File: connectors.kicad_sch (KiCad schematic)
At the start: 22 parts, among them J1 RPi_GPIO, J10 ToF1_Sensor, J11 ToF2_Sensor, J12 ToF3_Sensor, J13 ToF4_Sensor, J14 ToF5_Sensor, J15 ToF6_Sensor, J16 SPI_Interface, J17 UART_Interface, J18 Fan_Interface, J2 Motor_L, J3 Motor_R, J4 B_Cell_3, J5 B_Cell_2, J6 B_Cell_1, J7 SW, J8 Temp_Sensor, J9 IMU_Sensor

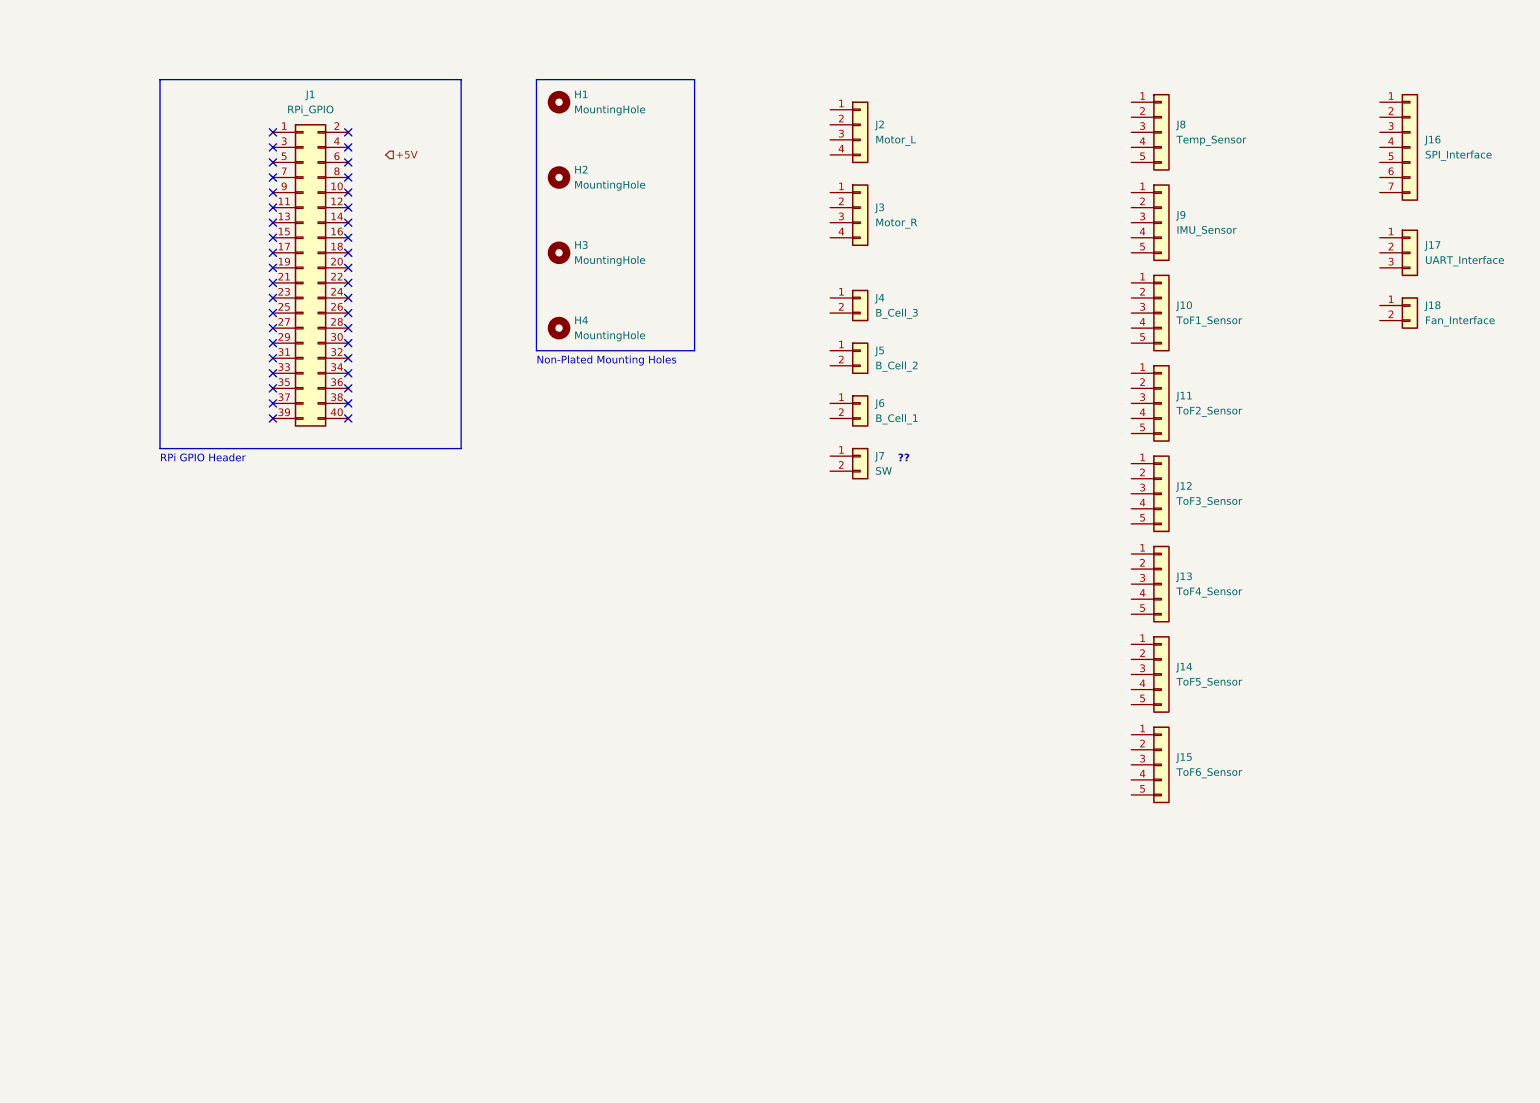
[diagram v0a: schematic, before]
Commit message: Finished motor drivers schematic
Still need to connect all the connectors and sort out old unused connections
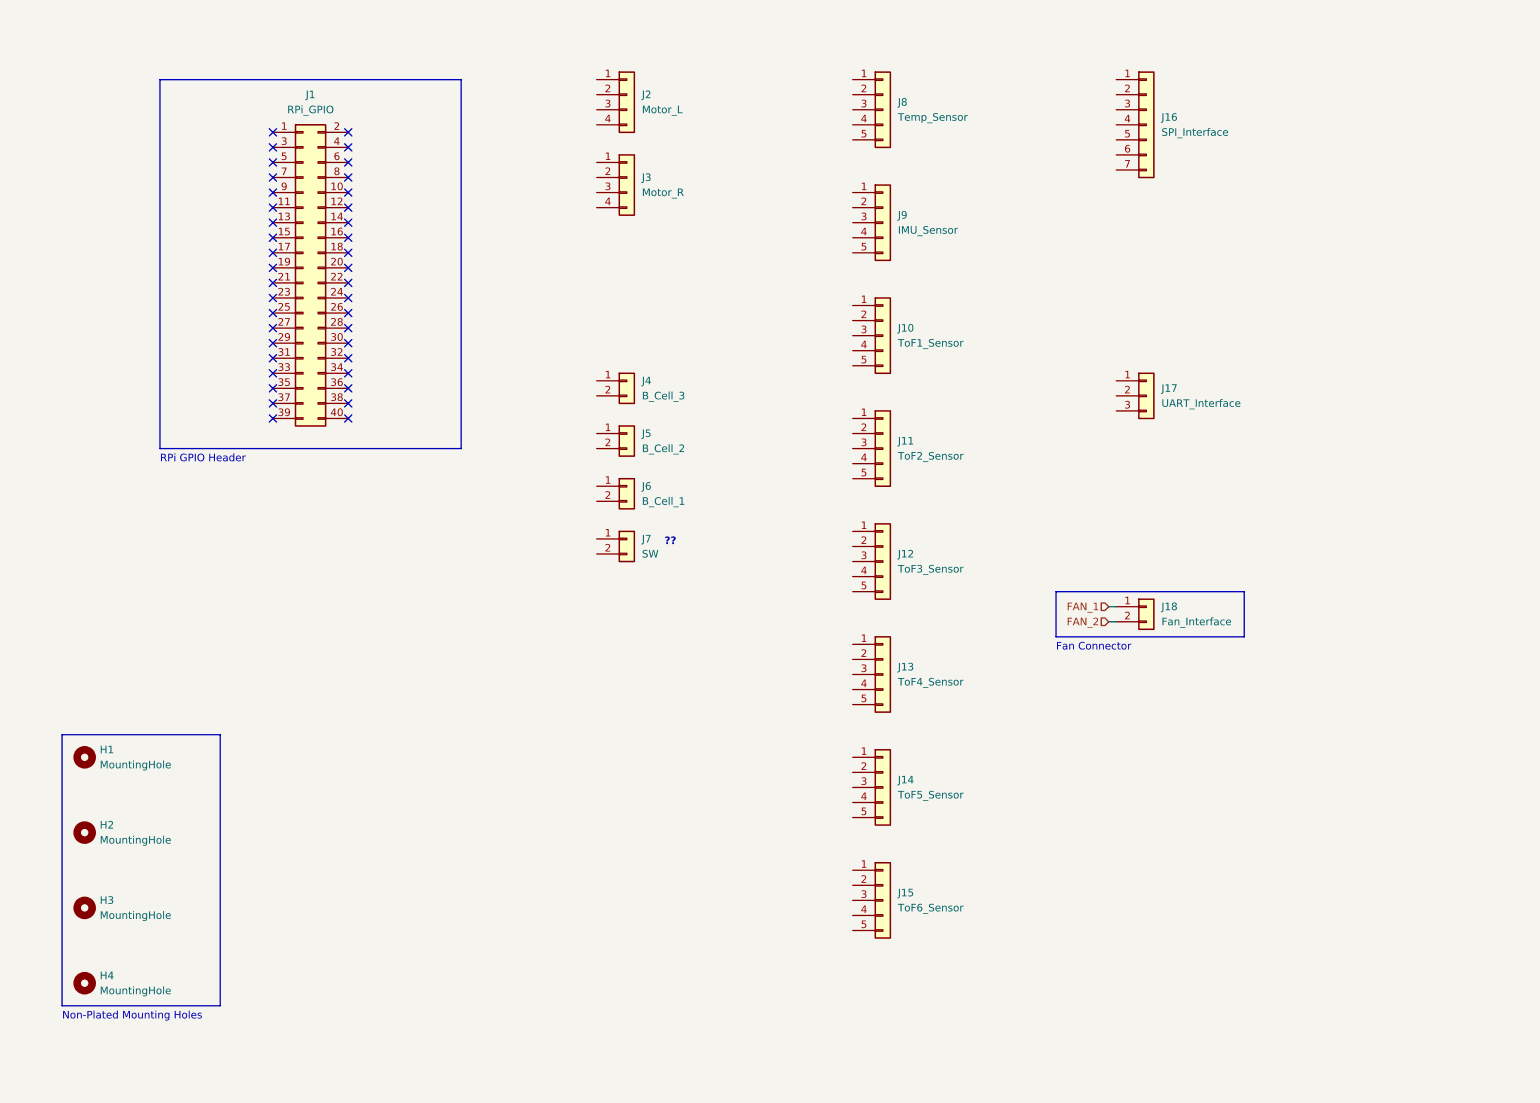
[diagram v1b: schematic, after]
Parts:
- J10, J11, J12, J13, J14, J15, J8, J9: footprint Connector_Molex:Molex_PicoBlade_53047-0510_1x05_P1.25mm_Vertical -> parts:SHDR5W27P0X125_1X5_800X320X440P
- J16: footprint Connector_Molex:Molex_PicoBlade_53047-0710_1x07_P1.25mm_Vertical -> parts:530470710
- J2, J3: footprint Connector_Molex:Molex_Micro-Fit_3.0_43650-0415_1x04_P3.00mm_Vertical -> parts:43650-04YY_151617
- J4, J5, J6, J7: footprint Connector_Molex:Molex_Micro-Fit_3.0_43045-0212_2x01_P3.00mm_Vertical -> parts:43045-02YY_121314
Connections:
- net FAN_1: now reaches J18.1 (Pin_1)
- net FAN_2: now reaches J18.2 (Pin_2)
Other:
- note added: "Fan Connector"
- title: Raspberry Pi Hat Module Connectors -> Interface Connectors
- moved on the sheet: H1, H2, H3, H4, J10, J11, J12, J13, J14, J15, J16, J17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

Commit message: New complete schematic version
May need to resize the resistors, also need to change the caps back to electrolytic
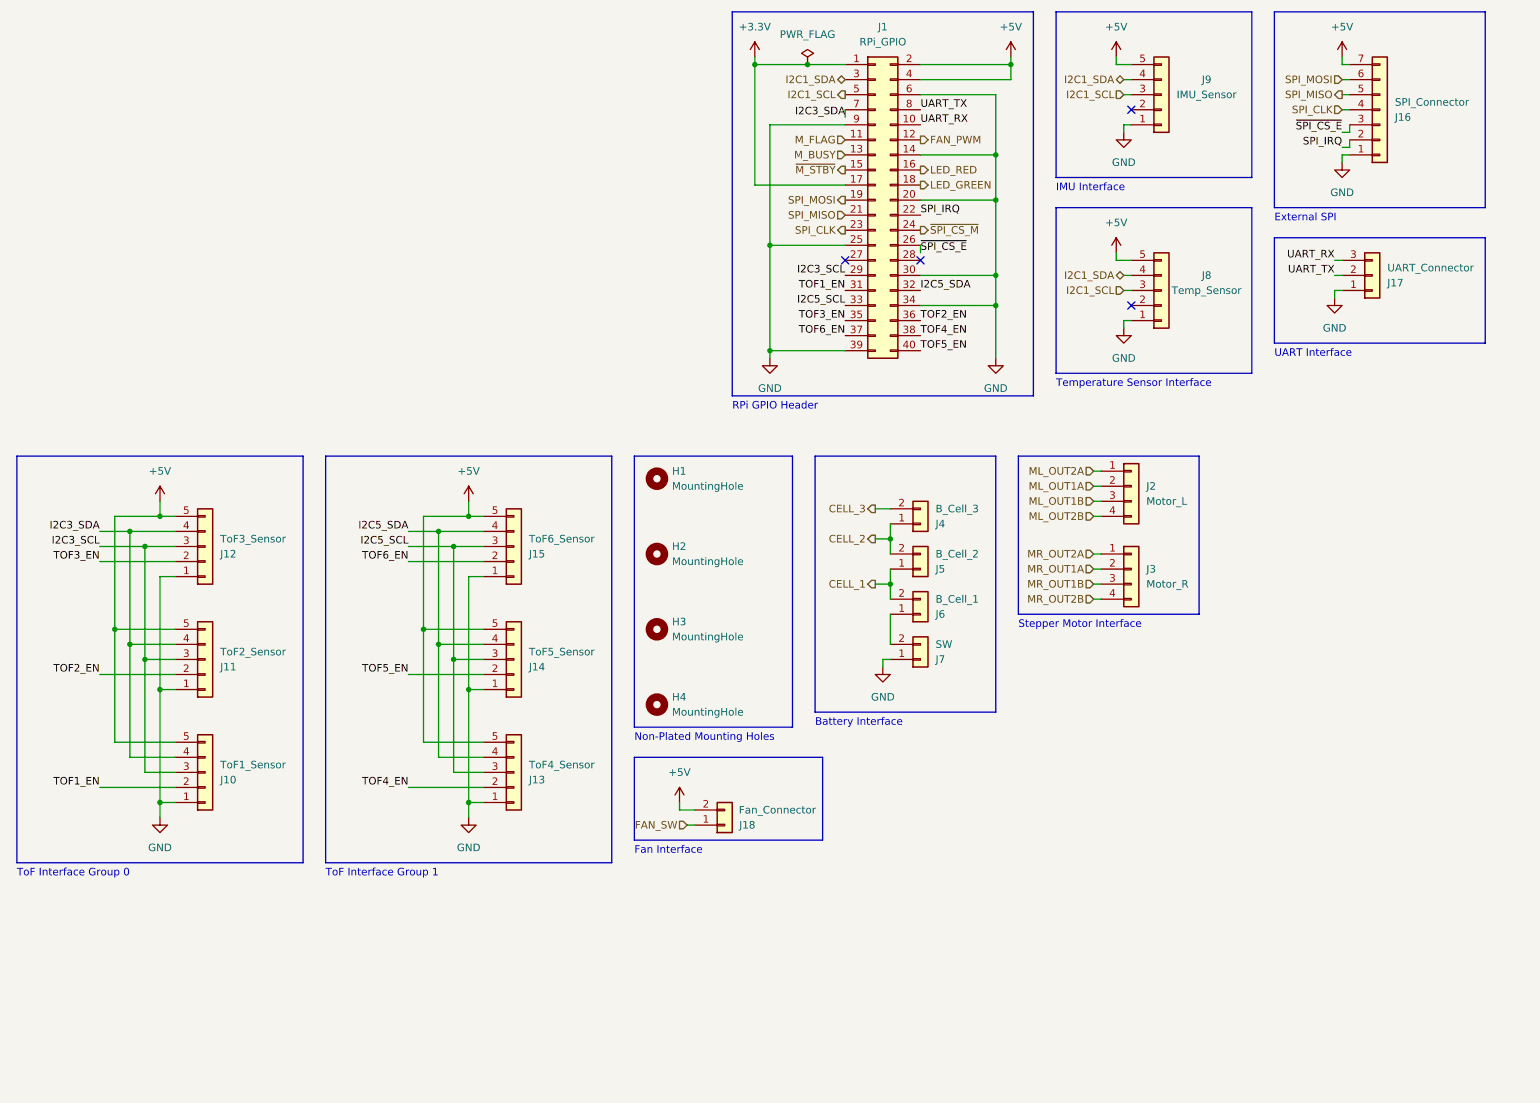
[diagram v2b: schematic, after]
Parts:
- J16: value SPI_Interface -> SPI_Connector
- J17: value UART_Interface -> UART_Connector
- J18: value Fan_Interface -> Fan_Connector
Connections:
- net FAN_2 is gone; now on net +5V: J18.2 (Pin_2)
- net ML_OUT2A: now reaches J2.1 (Pin_1)
- net ML_OUT1A: now reaches J2.2 (Pin_2)
- net ML_OUT1B: now reaches J2.3 (Pin_3)
- net ML_OUT2B: now reaches J2.4 (Pin_4)
- net GND: now reaches J15.1 (Pin_1)
- net GND: now also J1.14 (Pin_14), J1.20 (Pin_20), J1.25 (Pin_25), J1.30 (Pin_30), J1.34 (Pin_34), J1.39 (Pin_39), J1.6 (Pin_6), J1.9 (Pin_9), J10.1 (Pin_1), J11.1 (Pin_1), J12.1 (Pin_1), J13.1 (Pin_1), J14.1 (Pin_1), J16.1 (Pin_1), J17.1 (Pin_1), J7.1 (Pin_1), J8.1 (Pin_1), J9.1 (Pin_1)
- net TOF6_EN: now reaches J15.2 (Pin_2)
- net TOF6_EN: now also J1.37 (Pin_37)
- net I2C5_SCL: now reaches J15.3 (Pin_3)
- net I2C5_SCL: now also J1.33 (Pin_33), J13.3 (Pin_3), J14.3 (Pin_3)
- net I2C5_SDA: now reaches J15.4 (Pin_4)
- net I2C5_SDA: now also J1.32 (Pin_32), J13.4 (Pin_4), J14.4 (Pin_4)
- net +5V: now reaches J15.5 (Pin_5)
- net +5V: now also J1.2 (Pin_2), J1.4 (Pin_4), J10.5 (Pin_5), J11.5 (Pin_5), J12.5 (Pin_5), J13.5 (Pin_5), J14.5 (Pin_5), J16.7 (Pin_7), J8.5 (Pin_5), J9.5 (Pin_5)
- net TOF4_EN: now reaches J13.2 (Pin_2)
- net TOF4_EN: now also J1.38 (Pin_38)
- net +3.3V: now reaches J1.1 (Pin_1)
- net +3.3V: now also J1.17 (Pin_17)
- net UART_RX: now reaches J1.10 (Pin_10)
- net UART_RX: now also J17.3 (Pin_3)
- net M_FLAG: now reaches J1.11 (Pin_11)
- net FAN_PWM: now reaches J1.12 (Pin_12)
- net M_BUSY: now reaches J1.13 (Pin_13)
- net ~{M_STBY}: now reaches J1.15 (Pin_15)
- net LED_RED: now reaches J1.16 (Pin_16)
- net LED_GREEN: now reaches J1.18 (Pin_18)
- net SPI_MOSI: now reaches J1.19 (Pin_19)
- net SPI_MOSI: now also J16.6 (Pin_6)
- net SPI_MISO: now reaches J1.21 (Pin_21)
- net SPI_MISO: now also J16.5 (Pin_5)
- net SPI_IRQ: now reaches J1.22 (Pin_22)
- net SPI_IRQ: now also J16.2 (Pin_2)
- net SPI_CLK: now reaches J1.23 (Pin_23)
- net SPI_CLK: now also J16.4 (Pin_4)
- net ~{SPI_CS_M}: now reaches J1.24 (Pin_24)
- net ~{SPI_CS_E}: now reaches J1.26 (Pin_26)
- net ~{SPI_CS_E}: now also J16.3 (Pin_3)
- net I2C3_SCL: now reaches J1.29 (Pin_29)
- net I2C3_SCL: now also J10.3 (Pin_3), J11.3 (Pin_3), J12.3 (Pin_3)
- net I2C1_SDA: now reaches J1.3 (Pin_3)
- net I2C1_SDA: now also J8.4 (Pin_4), J9.4 (Pin_4)
- net TOF1_EN: now reaches J1.31 (Pin_31)
- net TOF1_EN: now also J10.2 (Pin_2)
- net TOF3_EN: now reaches J1.35 (Pin_35)
- net TOF3_EN: now also J12.2 (Pin_2)
- net TOF2_EN: now reaches J1.36 (Pin_36)
- net TOF2_EN: now also J11.2 (Pin_2)
- net TOF5_EN: now reaches J1.40 (Pin_40)
- net TOF5_EN: now also J14.2 (Pin_2)
- net I2C1_SCL: now reaches J1.5 (Pin_5)
- net I2C1_SCL: now also J8.3 (Pin_3), J9.3 (Pin_3)
- net I2C3_SDA: now reaches J1.7 (Pin_7)
- net I2C3_SDA: now also J10.4 (Pin_4), J11.4 (Pin_4), J12.4 (Pin_4)
- net UART_TX: now reaches J1.8 (Pin_8)
- net UART_TX: now also J17.2 (Pin_2)
- net at J6.1 (Pin_1): now also J7.2 (Pin_2)
- net CELL_1: now reaches J6.2 (Pin_2)
- net CELL_1: now also J5.1 (Pin_1)
- net MR_OUT2A: now reaches J3.1 (Pin_1)
- net MR_OUT1A: now reaches J3.2 (Pin_2)
- net MR_OUT1B: now reaches J3.3 (Pin_3)
- net MR_OUT2B: now reaches J3.4 (Pin_4)
- net CELL_2: now reaches J5.2 (Pin_2)
- net CELL_2: now also J4.1 (Pin_1)
- net CELL_3: now reaches J4.2 (Pin_2)
- net FAN_1 renamed FAN_SW
- no-connect marks 40 -> 4
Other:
- note added: "Battery Interface"
- note added: "External SPI"
- note added: "Fan Interface"
- note added: "IMU Interface"
- note added: "Stepper Motor Interface"
- note added: "Temperature Sensor Interface"
- note added: "ToF Interface Group 0"
- note added: "ToF Interface Group 1"
- note added: "UART Interface"
- note removed: "??"
- note removed: "Fan Connector"
- moved on the sheet: H1, H2, H3, H4, J1, J10, J11, J12, J13, J14, J15, J16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

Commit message: Uploaded all project files, finished PCB design
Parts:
- added F1: 10A Fuse, parts:FUSC6126X270N, symbol Device:Fuse
- H1, H2, H3, H4: now left out of the parts list
- J17: footprint Connector_PinHeader_2.54mm:PinHeader_1x03_P2.54mm_Vertical -> parts:SHDR5W27P0X125_1X5_800X320X440P; symbol Connector_Generic:Conn_01x03 -> Connector_Generic:Conn_01x05
- J18: footprint Connector_PinHeader_2.54mm:PinHeader_1x02_P2.54mm_Vertical -> Connector_PinHeader_2.54mm:PinHeader_1x02_P2.54mm_Vertical_SMD_Pin1Left
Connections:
- net +5V: now also J17.5 (Pin_5)
- net CELL_3: now also F1.2
- net UART_RX: now also J17.4 (Pin_4); no longer J17.3 (Pin_3)
- net UART_TX: now also J17.3 (Pin_3); no longer J17.2 (Pin_2)
- new net VCC: F1.1
- no-connect marks 4 -> 5
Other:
- moved on the sheet: J16, J18, J2, J3, J4, J8, J9

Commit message: Trace routing corrections, prepared for further modifications
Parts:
- J8: footprint parts:SHDR5W27P0X125_1X5_800X320X440P -> parts:530470510
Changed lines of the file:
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@@
       (effects (font (size 1.27 1.27)))
     )
-    (property "Footprint" "parts:SHDR5W27P0X125_1X5_800X320X440P" (at 31.75 179.07 0)
+    (property "Footprint" "parts:530470510" (at 31.75 179.07 0)
       (effects (font (size 1.27 1.27)) hide)
     )

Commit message: Fixed outdated connector footprints
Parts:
- J10, J11, J12, J13, J14, J15, J17, J9: footprint parts:SHDR5W27P0X125_1X5_800X320X440P -> parts:530470510
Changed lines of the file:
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@@
       (effects (font (size 1.27 1.27)) (justify left))
     )
-    (property "Footprint" "parts:SHDR5W27P0X125_1X5_800X320X440P" (at 97.79 104.14 0)
+    (property "Footprint" "parts:530470510" (at 97.79 104.14 0)
       (effects (font (size 1.27 1.27)) hide)
     )
@@
       (effects (font (size 1.27 1.27)) (justify left))
     )
-    (property "Footprint" "parts:SHDR5W27P0X125_1X5_800X320X440P" (at 97.79 142.24 0)
+    (property "Footprint" "parts:530470510" (at 97.79 142.24 0)
       (effects (font (size 1.27 1.27)) hide)
     )
@@
       (effects (font (size 1.27 1.27)) (justify left))
     )
-    (property "Footprint" "parts:SHDR5W27P0X125_1X5_800X320X440P" (at 102.87 179.07 0)
+    (property "Footprint" "parts:530470510" (at 102.87 179.07 0)
       (effects (font (size 1.27 1.27)) hide)
     )
@@
       (effects (font (size 1.27 1.27)) (justify left))
     )
-    (property "Footprint" "parts:SHDR5W27P0X125_1X5_800X320X440P" (at 45.72 104.14 0)
+    (property "Footprint" "parts:530470510" (at 45.72 104.14 0)
       (effects (font (size 1.27 1.27)) hide)
     )
@@
       (effects (font (size 1.27 1.27)) (justify left))
     )
-    (property "Footprint" "parts:SHDR5W27P0X125_1X5_800X320X440P" (at 97.79 123.19 0)
+    (property "Footprint" "parts:530470510" (at 97.79 123.19 0)
       (effects (font (size 1.27 1.27)) hide)
     )
@@
       (effects (font (size 1.27 1.27)) (justify left))
     )
-    (property "Footprint" "parts:SHDR5W27P0X125_1X5_800X320X440P" (at 45.72 142.24 0)
+    (property "Footprint" "parts:530470510" (at 45.72 142.24 0)
       (effects (font (size 1.27 1.27)) hide)
     )
@@
       (effects (font (size 1.27 1.27)) (justify left))
     )
-    (property "Footprint" "parts:SHDR5W27P0X125_1X5_800X320X440P" (at 45.72 123.19 0)
+    (property "Footprint" "parts:530470510" (at 45.72 123.19 0)
       (effects (font (size 1.27 1.27)) hide)
     )
@@
       (effects (font (size 1.27 1.27)))
     )
-    (property "Footprint" "parts:SHDR5W27P0X125_1X5_800X320X440P" (at 68.58 179.07 0)
-      (effects (font (size 1.27 1.27)) hide)
-    )
+    (property "Footprint" "parts:530470510" (at 68.58 179.07 0)
+      (effects (font (size 1.27 1.27)) hide)
+    )

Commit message: Changed fan connector type to THT
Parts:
- J18: footprint Connector_PinHeader_2.54mm:PinHeader_1x02_P2.54mm_Vertical_SMD_Pin1Left -> Connector_PinHeader_2.54mm:PinHeader_1x02_P2.54mm_Vertical
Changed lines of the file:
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@@
       (effects (font (size 1.27 1.27)))
     )
-    (property "Footprint" "Connector_PinHeader_2.54mm:PinHeader_1x02_P2.54mm_Vertical_SMD_Pin1Left" (at 134.62 153.67 0)
+    (property "Footprint" "Connector_PinHeader_2.54mm:PinHeader_1x02_P2.54mm_Vertical" (at 134.62 153.67 0)
       (effects (font (size 1.27 1.27)) hide)
     )
